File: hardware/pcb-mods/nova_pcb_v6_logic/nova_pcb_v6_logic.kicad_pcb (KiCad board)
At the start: 4 copper layers, 84 x 78 mm, 14 parts, among them J10 SSD1331_OLED, J11 WS2812B_Strip, J20 IB_2x06, J9 FE-URT-1, U12 Arduino_Nano_v3.x, U6 Teensy4.1, U7 74HC125

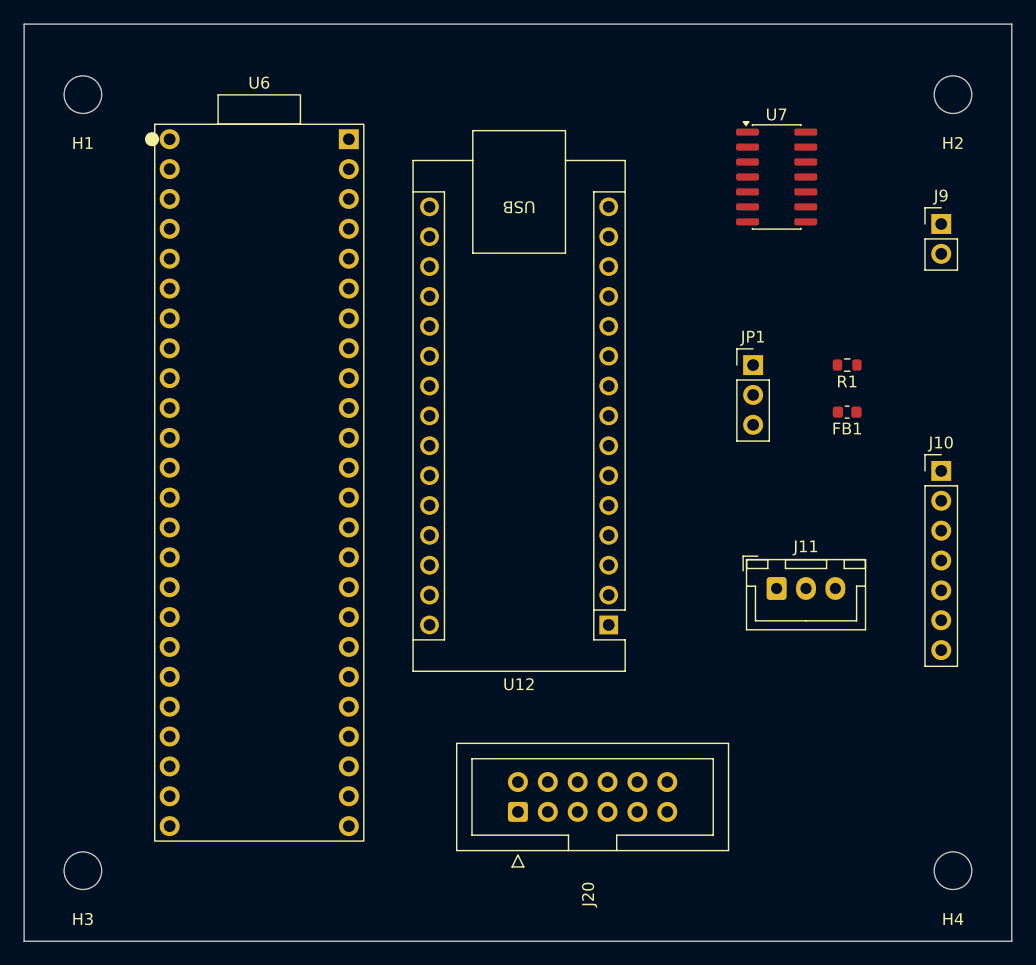
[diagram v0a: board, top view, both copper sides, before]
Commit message: pcb(v6-power-v2): fork to v2 — full reroute, safety chain, off-board INA226, DRC clean
- Fork nova_pcb_v6_power -> _v2 (v1 frozen); placement redone power-flow-first
- Safety chain board sync: Q3 e-stop inverter, Q4 EN_JET cutoff, R16, C8/C9
- INA226 modules converted off-board: footprints stripped to 4-pin I2C headers,
  RAW nets eliminated (bench wiring card in ROUTING_HANDOFF.md Step 8)
- All power routed 1.5/3.0mm per netclass, LEG pour L-shape, hip doubled F+B
- All signal nets routed headless via pre-commit collision checker:
  B.Cu lanes y137.5-139.9 + F.Cu verticals + via pairs; V5_AUX spine gap
  bridged x114.5; board min via relaxed to 0.45/0.25 (PCBWay standard)
- DRC: 0 errors, 0 unrouted; 2 zone-island seams left for GUI (Step 9)

Co-Authored-By: Claude Fable 5 <noreply@anthropic.com>
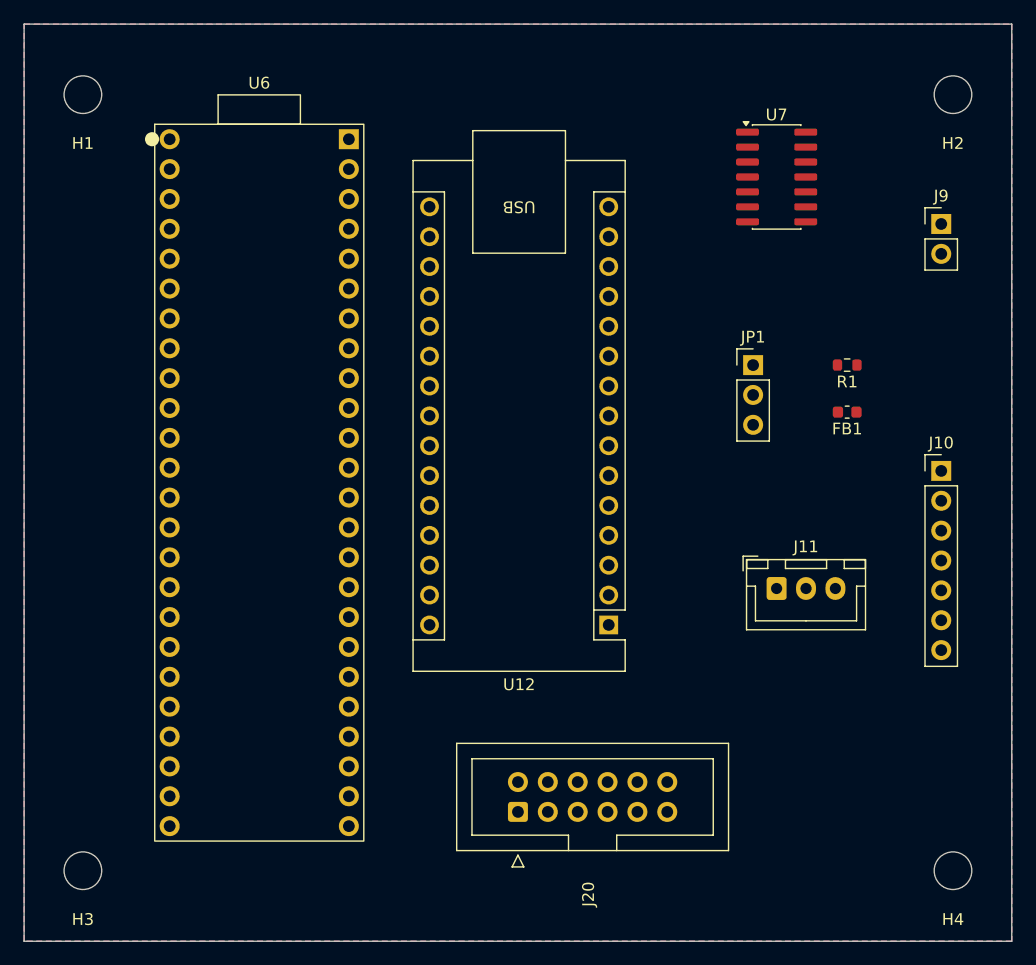
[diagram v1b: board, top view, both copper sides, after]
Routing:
- added copper zone on B.Cu, net GND
- added copper zone on F.Cu, net GND
- added copper zone on In1.Cu, net GND
- added copper zone on In2.Cu, net V5_AUX
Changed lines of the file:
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@@
 		(layer "Edge.Cuts")
+	)
+	(zone
+		(net 3)
+		(net_name "GND")
+		(layer "F.Cu")
+		(hatch edge 0.5)
+		(connect_pads
+			(clearance 0.3)
+		)
+		(min_thickness 0.25)
+		(filled_areas_thickness no)
+		(fill yes
+			(thermal_gap 0.3)
+			(thermal_bridge_width 0.5)
+		)
+		(polygon
+			(pts
+				(xy 98 57) (xy 182 57) (xy 182 135) (xy 98 135)
+			)
+		)
+	)
+	(zone
+		(net 3)
+		(net_name "GND")
+		(layer "B.Cu")
+		(hatch edge 0.5)
+		(connect_pads
+			(clearance 0.3)
+		)
+		(min_thickness 0.25)
+		(filled_areas_thickness no)
+		(fill yes
+			(thermal_gap 0.3)
+			(thermal_bridge_width 0.5)
+		)
+		(polygon
+			(pts
+				(xy 98 57) (xy 182 57) (xy 182 135) (xy 98 135)
+			)
+		)
+	)
+	(zone
+		(net 3)
+		(net_name "GND")
+		(layer "In1.Cu")
+		(hatch edge 0.5)
+		(connect_pads
+			(clearance 0.3)
+		)
+		(min_thickness 0.25)
+		(filled_areas_thickness no)
+		(fill yes
+			(thermal_gap 0.3)
+			(thermal_bridge_width 0.5)
+		)
+		(polygon
+			(pts
+				(xy 98 57) (xy 182 57) (xy 182 135) (xy 98 135)
+			)
+		)
+	)
+	(zone
+		(net 11)
+		(net_name "V5_AUX")
+		(layer "In2.Cu")
+		(hatch edge 0.5)
+		(connect_pads
+			(clearance 0.3)
+		)
+		(min_thickness 0.25)
+		(filled_areas_thickness no)
+		(fill yes
+			(thermal_gap 0.3)
+			(thermal_bridge_width 0.5)
+		)
+		(polygon
+			(pts
+				(xy 98 57) (xy 182 57) (xy 182 135) (xy 98 135)
+			)
+		)
 	)
 	(embedded_fonts no)

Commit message: fix(logic): +3V3 sourced from Teensy 3.3V (T3V3O pin added) — board-killer bug fixed
Netlist verified: +3V3 = [U6.T3V3O(3V3), U7.10/13/14(VCC), J20.5]. 74HC125
+ 3x INA226 now powered. Combined with R1/FB1 un-DNP, both logic-board
bugs from the 2026-06-13 review are resolved. Board left unrouted-clean
for autorouting (Freerouting).

Co-Authored-By: Claude Fable 5 <noreply@anthropic.com>
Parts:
- FB1: value FB_DNP -> Ferrite_600R
- R1: value 22R_DNP -> 22R
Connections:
- U6 pad T3V3O: (no net) -> +3V3
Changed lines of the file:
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@@
 			)
 		)
-		(property "Value" "22R_DNP"
+		(property "Value" "22R"
 			(at 0 1.43 0)
 			(layer "F.Fab")
@@
 		(sheetname "/05 Bus Integrity/")
 		(sheetfile "05_bus_integrity.kicad_sch")
-		(attr smd dnp)
+		(attr smd)
 		(fp_line
 			(start -0.237258 0.5225)
@@
 			(layers "*.Cu" "*.Mask")
 			(remove_unused_layers no)
+			(net 14 "+3V3")
+			(pinfunction "3V3")
+			(pintype "power_out")
 		)
 		(pad "T5" thru_hole circle
@@
 			)
 		)
-		(property "Value" "FB_DNP"
+		(property "Value" "Ferrite_600R"
 			(at 0 1.43 0)
 			(layer "F.Fab")
@@
 		(sheetname "/05 Bus Integrity/")
 		(sheetfile "05_bus_integrity.kicad_sch")
-		(attr smd dnp)
+		(attr smd)
 		(fp_line
 			(start -0.162779 0.51)

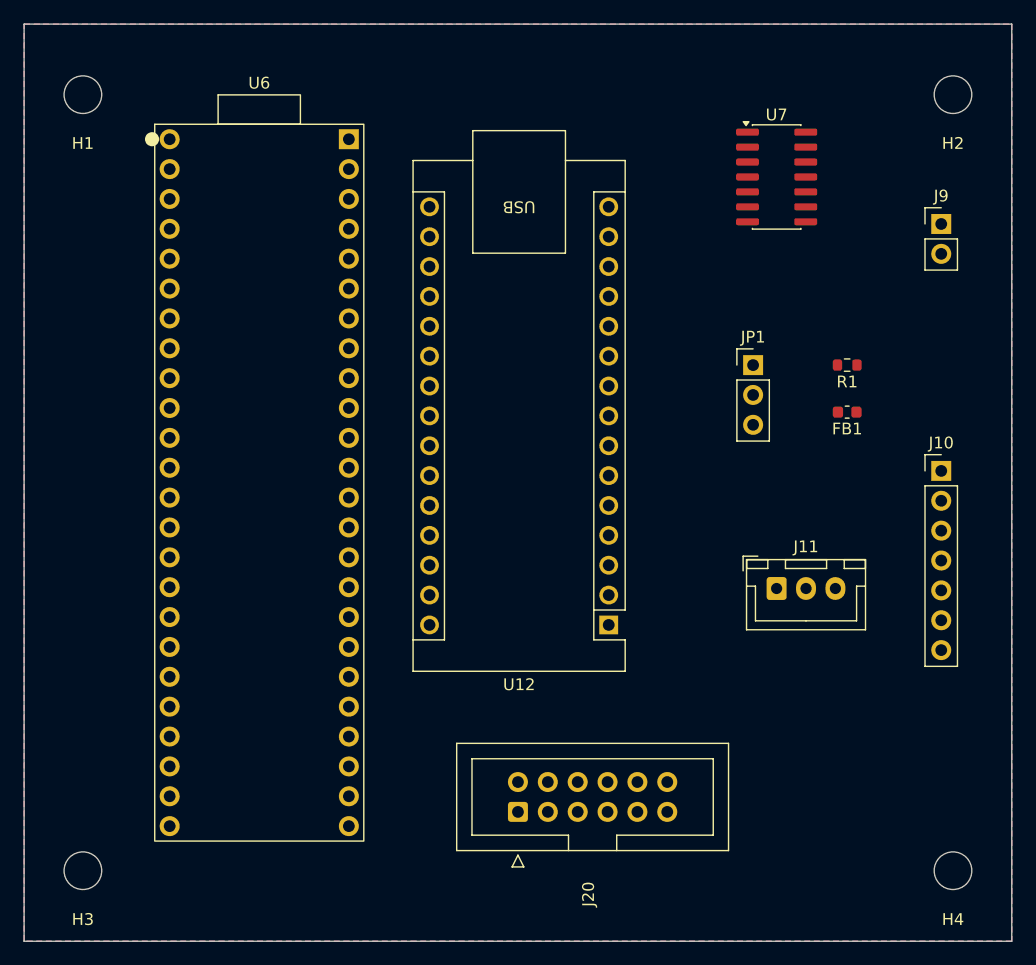
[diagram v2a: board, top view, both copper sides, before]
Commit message: pcb(logic): ROUTED via Freerouting — DRC 0 errors, 0 unconnected
24 nets autorouted (154 tracks, 3 vias) on the +3V3/R1/FB1-fixed netlist.
GND/V5_AUX inner planes filled. Min thermal spokes 2->1 to clear 4 GND
starved-thermal on Freerouting-packed pads (1-spoke relief fine + eases
hand-solder; pads also tie to inner GND plane). 7 cosmetic lib warnings.

Co-Authored-By: Claude Fable 5 <noreply@anthropic.com>
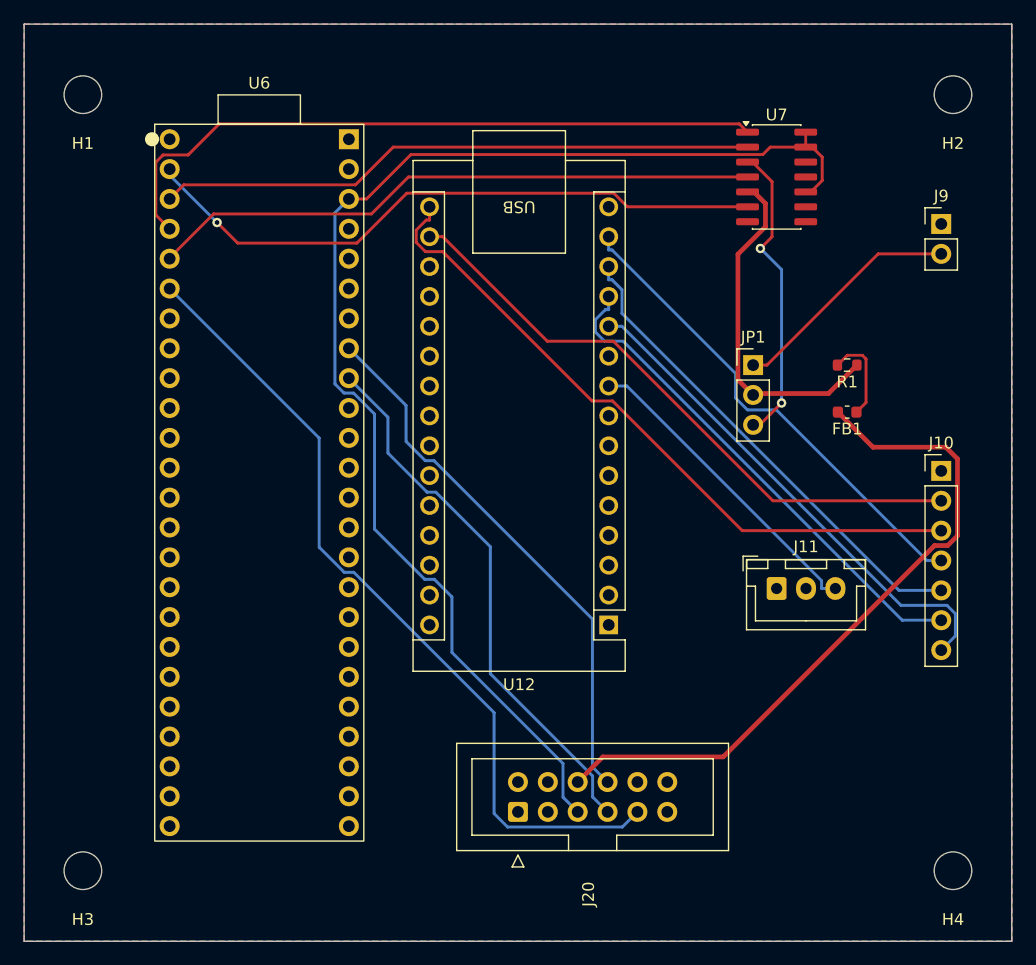
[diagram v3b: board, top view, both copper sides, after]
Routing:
- net +3V3: track 0.00 -> 109.6 mm
- net BATT_LOW: track 0.00 -> 69.7 mm
- net BUS_SERVO: track 0.00 -> 59.3 mm
- net /07 Aux MCU + Peripherals/SPI_SCK: track 0.00 -> 58.5 mm
- net /04 Bus Master (Pattern B)/OE_TX: track 0.00 -> 58.1 mm
- net /04 Bus Master (Pattern B)/TEENSY_RX: track 0.00 -> 54.3 mm, vias 0 -> 1
- net /07 Aux MCU + Peripherals/NANO_3V3: track 0.00 -> 52.8 mm
- net /04 Bus Master (Pattern B)/OE_RX: track 0.00 -> 52.1 mm
- net /04 Bus Master (Pattern B)/TEENSY_TX: track 0.00 -> 51.0 mm
- net I2C_SDA: track 0.00 -> 46.4 mm
- net I2C_SCL: track 0.00 -> 46.4 mm
- net /07 Aux MCU + Peripherals/OLED_DC: track 0.00 -> 43.2 mm
- net /07 Aux MCU + Peripherals/OLED_RST: track 0.00 -> 43.2 mm
- net /07 Aux MCU + Peripherals/SPI_MOSI: track 0.00 -> 41.6 mm
- net /07 Aux MCU + Peripherals/OLED_CS: track 0.00 -> 41.5 mm
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
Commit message: pcb(logic): add C1 100nF decoupling at U7 + re-route — DRC 0/0 COMPLETE
C1 (CC0603 100nF) across +3V3/GND placed next to U7 pin14; full board
re-routed via Freerouting (25 nets, 159 tracks, 2 vias). DRC: 0 errors,
0 unconnected. 7 cosmetic lib warnings. Logic board fab-ready.

Co-Authored-By: Claude Fable 5 <noreply@anthropic.com>
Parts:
- added C1: 100nF, Capacitor_SMD:C_0603_1608Metric, F.Cu at (166.2, 62.8)
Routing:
- net /04 Bus Master (Pattern B)/TEENSY_RX: track 54.3 -> 64.0 mm, vias 1 -> 0
- net /04 Bus Master (Pattern B)/TEENSY_TX: track 51.0 -> 57.8 mm
- net /04 Bus Master (Pattern B)/OE_TX: track 58.1 -> 61.0 mm
- net +3V3: track 109.6 -> 111.9 mm

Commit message: logic board: add e-stop sense to Teensy + reconcile firmware pins to board
Hardware e-stop (Q3) killed bucks autonomously but the Teensy was blind —
no ESTOP line crossed J20 (all 12 pins used). Added direct sense so the
SafetyFSM, /estop telemetry, and preflight can see e-stop state.

Board (nova_pcb_v6_logic):
- J21 (Conn_01x02) -> e-stop button 2nd NC dry contact -> Teensy pin 5
  (INPUT_PULLUP) + GND. NC-to-GND = LOW idle; pressed/break/unplug = HIGH
  = e-stop (fail-safe). Dry contact = no level-shift hazard.
- Routed F.Cu J21.1->U6.T5; existing 154 tracks untouched. DRC 0/0.
- Gerbers re-cut. No power-board / J20 change.

Firmware (teensy41_ci green) - pin defines reconciled to board routing
(old defines drove the wrong pins = dead bus):
- bus UART Serial2(7/8) -> Serial1(0/1)
- OE_TX/OE_RX 6/5 -> 2/3
- BATTERY_LOW 3 -> 4
- ESTOP 2 -> 5, polarity LOW->HIGH (NC fail-safe)
- I2C 18/19 unchanged (already matched)
SafetyFSM already latches e-stop until /safety_clear, so snap-back on
release is covered without an inference latch.

Co-Authored-By: Claude Opus 4.8 <noreply@anthropic.com>
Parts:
- added J21: Conn_01x02, Connector_PinHeader_2.54mm:PinHeader_1x02_P2.54mm_Vertical, F.Cu at (105.0, 82.2)
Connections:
- U6 pad T5: (no net) -> Net-(J21-Pin_1)
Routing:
- net Net-(J21-Pin_1): track 0.00 -> 5.38 mm
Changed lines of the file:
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@@
 	(net 43 "unconnected-(U12-A3-Pad22)")
 	(net 44 "unconnected-(U12-D7-Pad10)")
+	(net 45 "Net-(J21-Pin_1)")
 	(footprint "Connector_IDC:IDC-Header_2x06_P2.54mm_Vertical"
 		(layer "F.Cu")
@@
 		)
 	)
+	(footprint "Connector_PinHeader_2.54mm:PinHeader_1x02_P2.54mm_Vertical"
+		(layer "F.Cu")
+		(at 105 82.225)
+		(descr "Through hole straight pin header, 1x02, 2.54mm pitch, single row")
+		(tags "Through hole pin header THT 1x02 2.54mm single row")
+		(property "Reference" "J21"
+			(at 0 -2.38 0)
+			(layer "F.SilkS")
+			(effects
+				(font
+					(size 1 1)
+					(thickness 0.15)
+				)
+			)
+		)
+		(property "Value" "Conn_01x02"
+			(at 0 4.92 0)
+			(layer "F.Fab")
+			(effects
+				(font
+					(size 1 1)
+					(thickness 0.15)
+				)
+			)
+		)
+		(property "Datasheet" "~"
+			(at 0 0 0)
+			(layer "F.Fab")
+			(hide yes)
+			(effects
+				(font
+					(size 1.27 1.27)
+					(thickness 0.15)
+				)
+			)
+		)
+		(property "Description" "Generic connector, single row, 01x02, script generated (kicad-library-utils/schlib/autogen/connector/)"
+			(at 0 0 0)
+			(layer "F.Fab")
+			(hide yes)
+			(effects
+				(font
+					(size 1.27 1.27)
+					(thickness 0.15)
+				)
+			)
+		)
+		(property ki_fp_filters "Connector*:*_1x??_*")
+		(sheetname "/04 Bus Master (Pattern B)/")
+		(sheetfile "04_bus_master.kicad_sch")
+		(attr through_hole)
+		(fp_line
+			(start -1.38 -1.38)
+			(end 0 -1.38)
+			(stroke
+				(width 0.12)
+				(type solid)
+			)
+			(layer "F.SilkS")
+		)
+		(fp_line
+			(start -1.38 0)
+			(end -1.38 -1.38)
+			(stroke
+				(width 0.12)
+				(type solid)
+			)
+			(layer "F.SilkS")
+		)
+		(fp_line
+			(start -1.38 1.27)
+			(end -1.38 3.92)
+			(stroke
+				(width 0.12)
+				(type solid)
+			)
+			(layer "F.SilkS")
+		)
+		(fp_line
+			(start -1.38 1.27)
+			(end 1.38 1.27)
+			(stroke
+				(width 0.12)
+				(type solid)
+			)
+			(layer "F.SilkS")
+		)
+		(fp_line
+			(start -1.38 3.92)
+			(end 1.38 3.92)
+			(stroke
+				(width 0.12)
+				(type solid)
+			)
+			(layer "F.SilkS")
+		)
+		(fp_line
+			(start 1.38 1.27)
+			(end 1.38 3.92)
+			(stroke
+				(width 0.12)
+				(type solid)
+			)
+			(layer "F.SilkS")
+		)
+		(fp_line
+			(start -1.77 -1.77)
+			(end -1.77 4.32)
+			(stroke
+				(width 0.05)
+				(type solid)
+			)
+			(layer "F.CrtYd")
+		)
+		(fp_line
+			(start -1.77 4.32)
+			(end 1.77 4.32)
+			(stroke
+				(width 0.05)
+				(type solid)
+			)
+			(layer "F.CrtYd")
+		)
+		(fp_line
+			(start 1.77 -1.77)
+			(end -1.77 -1.77)
+			(stroke
+				(width 0.05)
+				(type solid)
+			)
+			(layer "F.CrtYd")
+		)
+		(fp_line
+			(start 1.77 4.32)
+			(end 1.77 -1.77)
+			(stroke
+				(width 0.05)
+				(type solid)
+			)
+			(layer "F.CrtYd")
+		)
+		(fp_line
+			(start -1.27 -0.635)
+			(end -0.635 -1.27)
+			(stroke
+				(width 0.1)
+				(type solid)
+			)
+			(layer "F.Fab")
+		)
+		(fp_line
+			(start -1.27 3.81)
+			(end -1.27 -0.635)
+			(stroke
+				(width 0.1)
+				(type solid)
+			)
+			(layer "F.Fab")
+		)
+		(fp_line
+			(start -0.635 -1.27)
+			(end 1.27 -1.27)
+			(stroke
+				(width 0.1)
+				(type solid)
+			)
+			(layer "F.Fab")
+		)
+		(fp_line
+			(start 1.27 -1.27)
+			(end 1.27 3.81)
+			(stroke
+				(width 0.1)
+				(type solid)
+			)
+			(layer "F.Fab")
+		)
+		(fp_line
+			(start 1.27 3.81)
+			(end -1.27 3.81)
+			(stroke
+				(width 0.1)
+				(type solid)
+			)
+			(layer "F.Fab")
+		)
+		(fp_text user "${REFERENCE}"
+			(at 0 1.27 90)
+			(layer "F.Fab")
+			(effects
+				(font
+					(size 1 1)
+					(thickness 0.15)
+				)
+			)
+		)
+		(pad "1" thru_hole rect
+			(at 0 0)
+			(size 1.7 1.7)
+			(drill 1)
+			(layers "*.Cu" "*.Mask")
+			(remove_unused_layers no)
+			(net 45 "Net-(J21-Pin_1)")
+			(pinfunction "Pin_1")
+			(pintype "passive")
+		)
+		(pad "2" thru_hole circle
+			(at 0 2.54)
+			(size 1.7 1.7)
+			(drill 1)
+			(layers "*.Cu" "*.Mask")
+			(remove_unused_layers no)
+			(net 3 "GND")
+			(pinfunction "Pin_2")
+			(pintype "passive")
+		)
+		(embedded_fonts no)
+		(model "${KICAD9_3DMODEL_DIR}/Connector_PinHeader_2.54mm.3dshapes/PinHeader_1x02_P2.54mm_Vertical.step"
+			(offset
+				(xyz 0 0 0)
+			)
+			(scale
+				(xyz 1 1 1)
+			)
+			(rotate
+				(xyz 0 0 0)
+			)
+		)
+	)
 	(footprint "Connector_PinHeader_2.54mm:PinHeader_1x07_P2.54mm_Vertical"
 		(layer "F.Cu")
@@
 			(layers "*.Cu" "*.Mask")
 			(remove_unused_layers no)
+			(net 45 "Net-(J21-Pin_1)")
+			(pintype "bidirectional")
 		)
 		(pad "T6" thru_hole circle
@@
 		(net 22)
 	)
+	(segment
+		(start 105 82.225)
+		(end 110.38 82.03)
+		(width 0.25)
+		(layer "F.Cu")
+		(net 45)
+	)
 	(zone

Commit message: logic board: fix OLED (J10) power/pinout/level + add series-R protection
Fresh full-board review surfaced 3 real OLED issues vs the owned HiLetgo
SSD1331 (7-pin, VCC 2.8-5.5V):

1. J10 pin order had CS/RST crossed vs the module -> swapped board nets
   (J10.5=OLED_RST, J10.7=OLED_CS).
2. Vcc was on NANO_3V3 (Nano onboard reg, <=50mA, often absent when the
   Nano runs off its 5V pin) -> moved to V5_AUX (5V; in module's range).
3. Nano runs at 5V, so its SPI logic over-drives the 3.3V-regulated
   SSD1331 inputs -> added 5x 1k series R (R2-R6) on SCK/MOSI/RST/DC/CS.

Schematic: Device:R lib symbol + R2-R6 + _F nets bridging U12->R->J10,
ERC clean of new items. PCB: full Freerouting re-route, GND via added to
restitch U7.7 to the inner plane, DRC 0/0, gerbers re-cut.

Also verified this pass: Teensy footprint pad->pin map (firmware pins
correct), bus Pattern B path, BATT_LOW cross-board (3.3V pull, correct
polarity), e-stop polarity consistent power<->logic. Both boards DRC 0/0.

Co-Authored-By: Claude Opus 4.8 <noreply@anthropic.com>
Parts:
- added R2: 1k, Resistor_SMD:R_0603_1608Metric, F.Cu at (168.2, 99.2)
- added R3: 1k, Resistor_SMD:R_0603_1608Metric, B.Cu at (166.6, 95.5)
- added R4: 1k, Resistor_SMD:R_0603_1608Metric, B.Cu at (169.2, 101.0)
- added R5: 1k, Resistor_SMD:R_0603_1608Metric, B.Cu at (167.7, 104.2)
- added R6: 1k, Resistor_SMD:R_0603_1608Metric, F.Cu at (171.7, 110.8)
- moved J11 5.25 mm to (156.8, 105.0)
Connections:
- J10 pad 2: /07 Aux MCU + Peripherals/NANO_3V3 -> V5_AUX
- J10 pad 3: /07 Aux MCU + Peripherals/SPI_SCK -> /07 Aux MCU + Peripherals/SPI_SCK_F
- J10 pad 4: /07 Aux MCU + Peripherals/SPI_MOSI -> /07 Aux MCU + Peripherals/SPI_MOSI_F
- J10 pad 5: /07 Aux MCU + Peripherals/OLED_CS -> /07 Aux MCU + Peripherals/OLED_RST_F
- J10 pad 6: /07 Aux MCU + Peripherals/OLED_DC -> /07 Aux MCU + Peripherals/OLED_DC_F
- J10 pad 7: /07 Aux MCU + Peripherals/OLED_RST -> /07 Aux MCU + Peripherals/OLED_CS_F
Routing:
- net /07 Aux MCU + Peripherals/NANO_3V3: track 52.8 -> 0.00 mm
- net BUS_SERVO: track 59.3 -> 40.6 mm
- net /07 Aux MCU + Peripherals/OLED_RST: track 43.2 -> 28.2 mm
- net /07 Aux MCU + Peripherals/SPI_MOSI: track 41.6 -> 29.8 mm
- net /07 Aux MCU + Peripherals/SPI_MOSI_F: track 0.00 -> 11.5 mm
- net /07 Aux MCU + Peripherals/OLED_DC: track 43.2 -> 33.6 mm
- net /04 Bus Master (Pattern B)/TEENSY_RX: track 64.0 -> 54.3 mm, vias 0 -> 1
- net /07 Aux MCU + Peripherals/OLED_CS: track 41.5 -> 50.9 mm, vias 0 -> 1
- net /07 Aux MCU + Peripherals/OLED_DC_F: track 0.00 -> 8.93 mm
- net /04 Bus Master (Pattern B)/OE_TX: track 61.0 -> 52.5 mm
- net /07 Aux MCU + Peripherals/OLED_RST_F: track 0.00 -> 7.72 mm
- net /07 Aux MCU + Peripherals/SPI_SCK_F: track 0.00 -> 7.27 mm
- net /07 Aux MCU + Peripherals/SPI_SCK: track 58.5 -> 53.0 mm
- net /07 Aux MCU + Peripherals/OLED_CS_F: track 0.00 -> 3.71 mm
- net /07 Aux MCU + Peripherals/LED_DATA: track 26.8 -> 23.2 mm
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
